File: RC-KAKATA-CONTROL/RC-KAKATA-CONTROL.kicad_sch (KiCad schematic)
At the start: 67 parts, among them J1 Conn_02x20_Socket_DG250T-5.0-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, J10 DB125-2.54-4P-GN, J12 Conn_01x07, J25 Conn_02x20_Socket_DG250T-5.0-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, J6 Raspberry_Pi_2x20_PTH, J8 DB125-2.54-4P-GN, U3 STM32H743IIT6, U8 W25Q128JVSIQTR, X1 SMD3225-4, X2 Q13MC3061000300

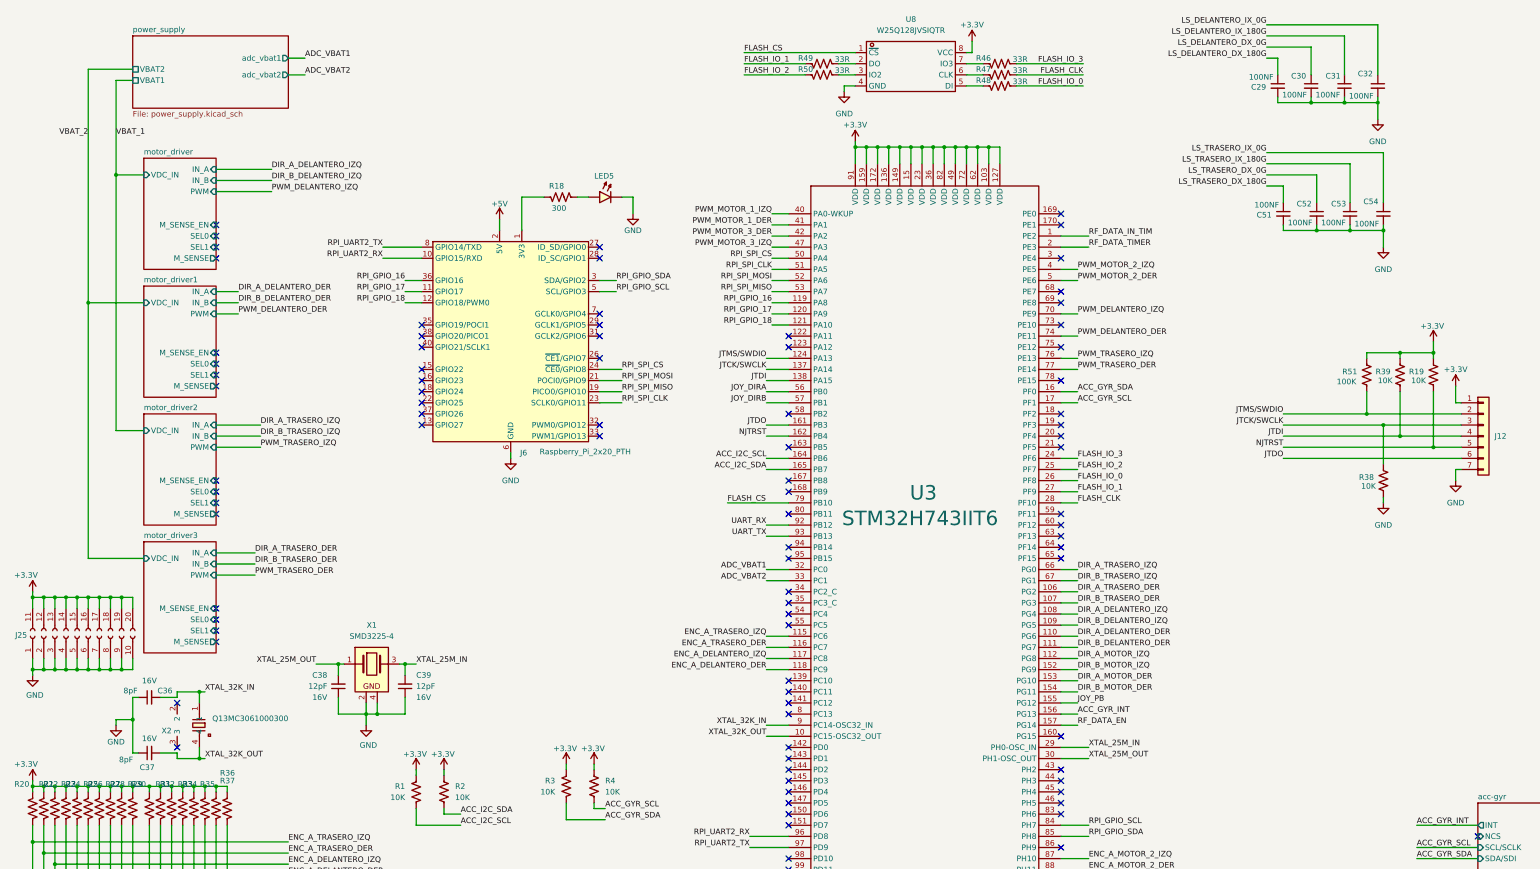
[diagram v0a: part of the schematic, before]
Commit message: Creadas Conexiones de GND y +3.3V Creada Conexion de +5 Creadas las conexiones criticas de Flash - SPI - I2C
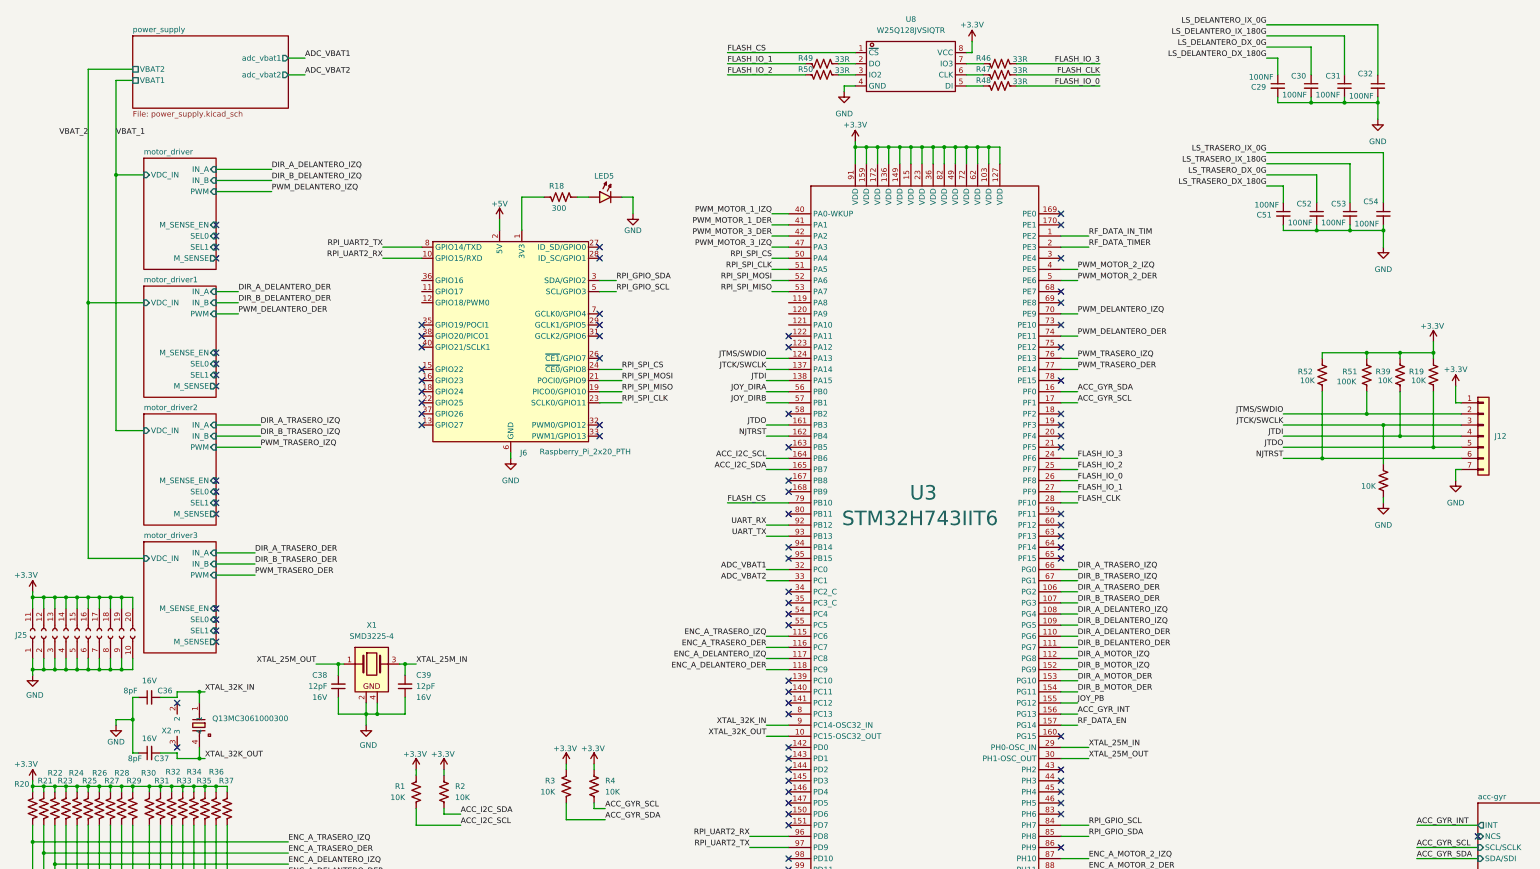
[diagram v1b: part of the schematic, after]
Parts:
- added R52: 10K, 4ms_Resistor:R_0603, symbol MG_RESISTOR:RES-0603-10K-1%
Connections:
- net +3.3V: now also R52.1
- net JTDO: now also J12.5 (Pin_5), R19.2; no longer J12.6 (Pin_6)
- net NJTRST: now also J12.6 (Pin_6), R52.2; no longer J12.5 (Pin_5), R19.2
- net RPI_GPIO_16: no longer names the net of U3.119 (PA8)
- net RPI_GPIO_16: no longer J6.36 (GPIO16)
- net RPI_GPIO_17: no longer names the net of U3.120 (PA9)
- net RPI_GPIO_17: no longer J6.11 (GPIO17)
- net RPI_GPIO_18: no longer names the net of U3.121 (PA10)
- net RPI_GPIO_18: no longer J6.12 (GPIO18/PWM0)

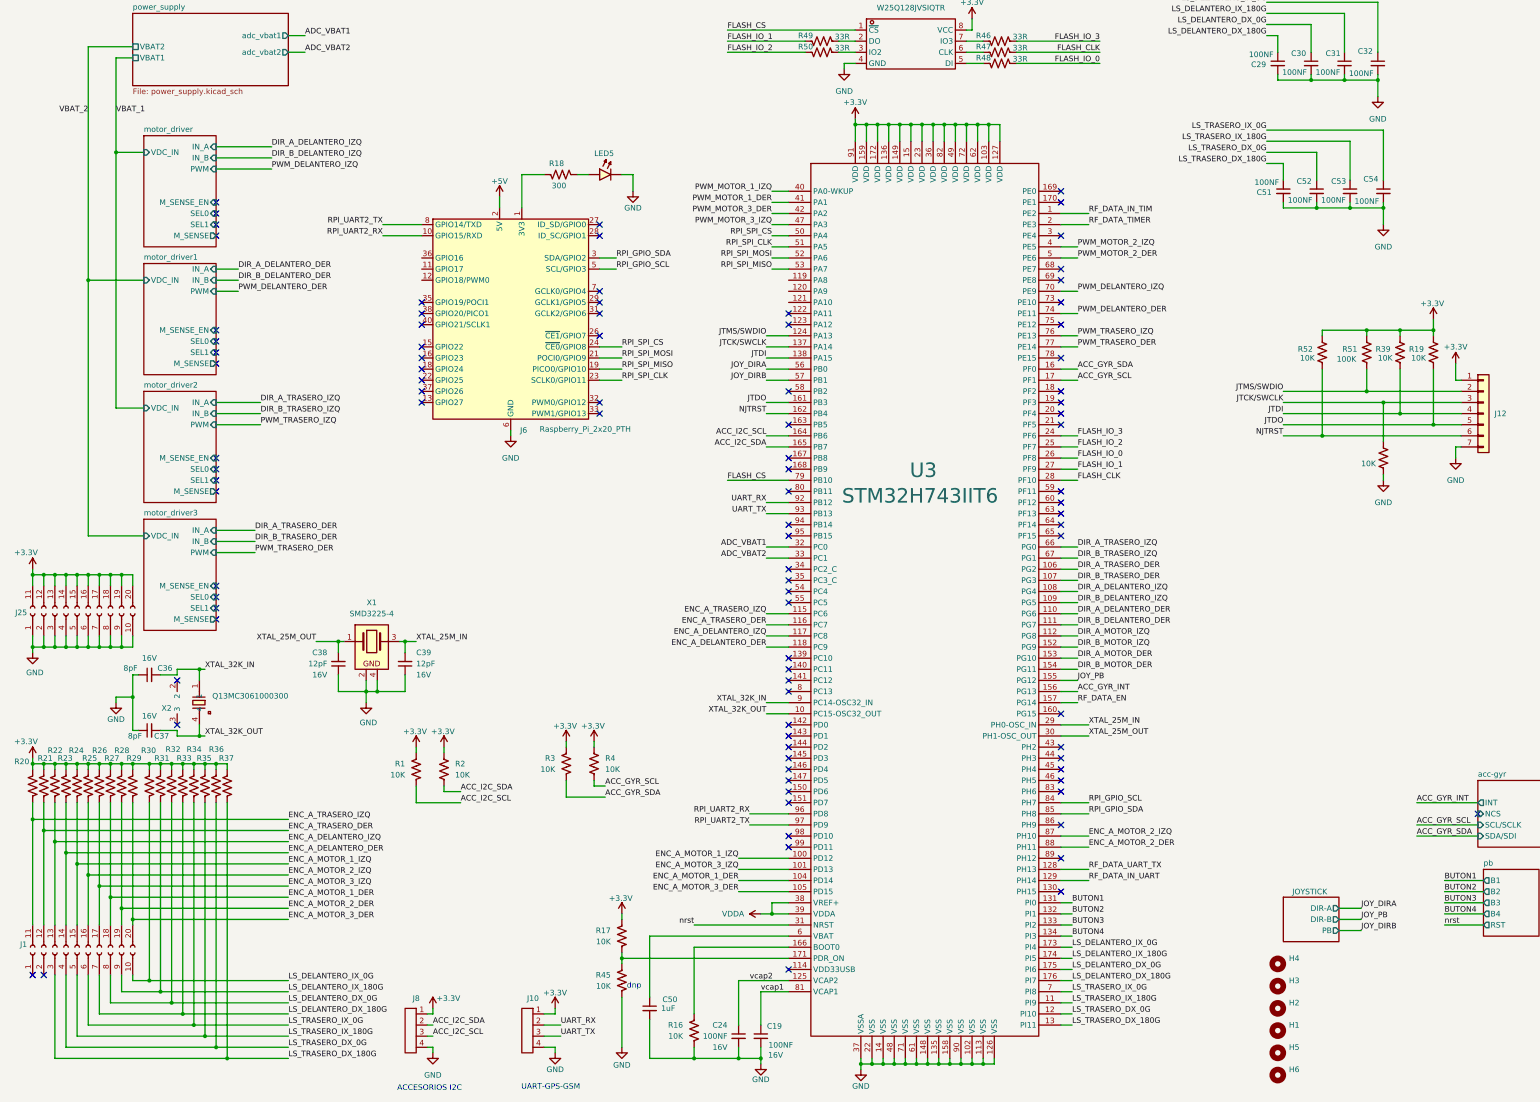
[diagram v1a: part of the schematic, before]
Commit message: Restan 32 pistas por rutear Colocados los Ref de los compoentes
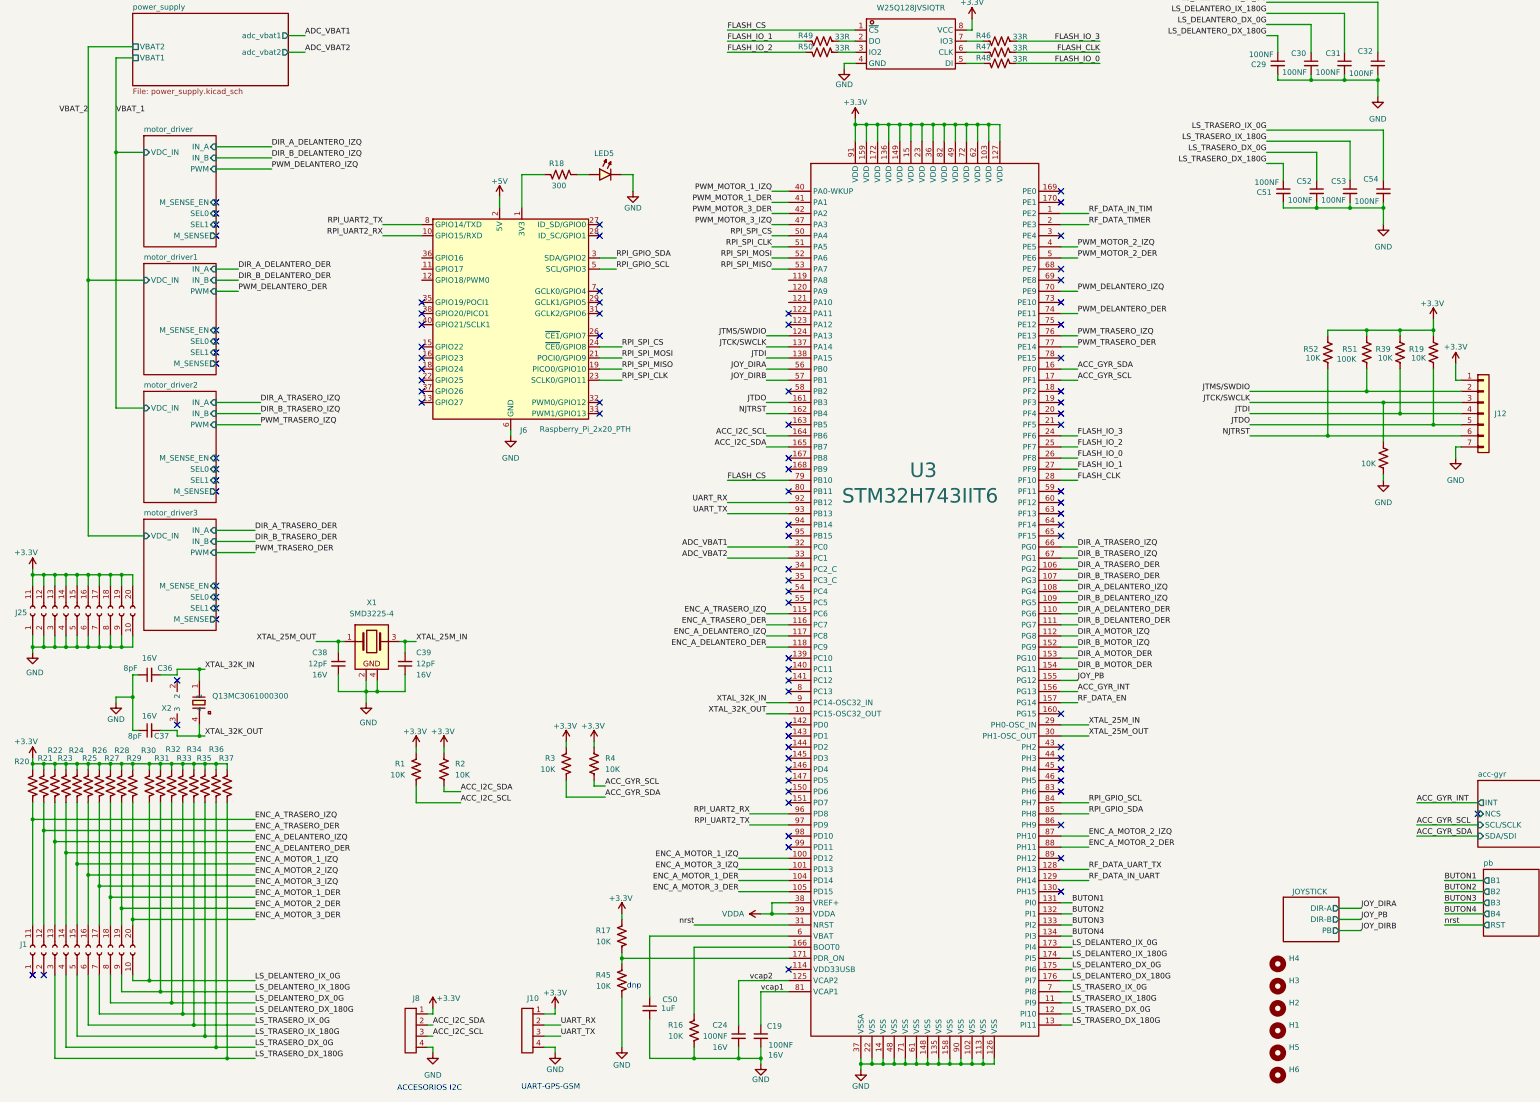
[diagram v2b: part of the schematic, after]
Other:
- moved on the sheet: R52

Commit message: Completado el BOM
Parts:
- added J14: DB125-2.54-4P-GN, EasyEDA:CONN-TH_DB125-2.54-4P-GN, symbol EasyEDA:DB125-2.54-4P-GN
- added R53, R54, R55: 22K, 4ms_Resistor:R_0603, symbol MG_RESISTOR:RES-0603-10K-1%
- added TP1, TP2, TP3, TP4, TP5: TestPoint_Hole1, 4ms_TestPoint:TestPoint_WireHole, symbol MG_ELECTROMECANICAL:TestPoint_Hole1
- C19, C24, C29, C30, C31, C32, C51, C52, C53, C54: LCSC Part (none) -> C14663
- C36: value 8pF -> 16pF; JLCPCB ID C14663 -> (none); LCSC Part (none) -> C327125
- C37: value 8pF -> 16pF; Display 0.1uF -> (none); JLCPCB ID C14663 -> (none); LCSC Part (none) -> C327125
- C38, C39: value 12pF -> 20pF; LCSC Part (none) -> C105621
- C50: LCSC Part (none) -> C559769
- J1, J25: now not fitted; now left out of the parts list
- J6: LCSC Part (none) -> C9138
- LED5: LCSC Part (none) -> C965799
- R1, R2, R3, R4: value 10K -> 4.7K; LCSC Part (none) -> C99782
- R16, R19, R38, R39, R52: LCSC Part (none) -> C98220
- R17: value 10K -> 22K; LCSC Part (none) -> C114065
- R18: LCSC Part (none) -> C114617
- R20, R21, R22, R23, R24, R25, R26, R27, R28, R29, R30, R31, R32, R33, R34, R35, R36, R37: LCSC Part (none) -> C114065
- R45: value 10K -> 22K; LCSC Part (none) -> C114065; now not fitted
- R46, R47, R48: LCSC Part (none) -> C108661
- R49, R50: LCSC Part (none) -> C108661; Part Number RC0603FR-0710KL -> RC0603FR-0733RL
- R51: LCSC Part (none) -> C14675
- U8: value W25Q128JVSIQTR -> W25Q128JVSIQ
- X1: value SMD3225-4 -> 25MHZ; LCSC Part (none) -> C5280577; PART_NUMBER (none) -> XL2EL89CSI-111YLC-25M
- X2: value Q13MC3061000300 -> 32.768kHz; PART_NUMBER (none) -> Q13MC30610003
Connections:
- net +3.3V: now also R53.1, R54.1, R55.1
- net GND: now also J14.4
- net at U3.59 (PF11): now also TP1.1
- net at U3.60 (PF12): now also TP2.1
- net at U3.63 (PF13): now also TP3.1
- net at U3.64 (PF14): now also TP4.1
- net at U3.65 (PF15): now also TP5.1
- net ACC_1: now reaches U3.94 (PB14)
- net ACC_1: now also J14.1, R55.2
- net ACC_2: now reaches U3.98 (PD10)
- net ACC_2: now also J14.2, R54.2
- net ACC_3: now reaches U3.99 (PD11)
- net ACC_3: now also J14.3, R53.2
- no-connect marks 116 -> 108

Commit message: V1.0 Enviada a fabricar
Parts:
- C36: JLCPCB ID (none) -> C14663
- C37: Display (none) -> 0.1uF; JLCPCB ID (none) -> C14663
- J12: LCSC Part (none) -> C6332200
- R49, R50: Part Number RC0603FR-0733RL -> RC0603FR-0710KL
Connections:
- no-connect marks 108 -> 113
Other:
- sheet acc-gyr ports: added SCL, SDA; removed NCS, SCL/SCLK, SDA/SDI
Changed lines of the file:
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@@
 	)
 	(no_connect
+		(at 107.95 81.28)
+	)
+	(no_connect
 		(at 52.07 172.72)
 	)
@@
 	)
 	(no_connect
+		(at 191.77 81.28)
+	)
+	(no_connect
 		(at 191.77 106.68)
 	)
@@
 	)
 	(no_connect
+		(at 107.95 78.74)
+	)
+	(no_connect
 		(at 191.77 129.54)
 	)
 	(no_connect
+		(at 191.77 86.36)
+	)
+	(no_connect
+		(at 191.77 83.82)
+	)
+	(no_connect
 		(at 107.95 86.36)
 	)
@@
 	)
 	(no_connect
-		(at 349.25 203.2)
-	)
-	(no_connect
 		(at 254 63.5)
 	)
@@
 	)
 	(no_connect
+		(at 107.95 76.2)
+	)
+	(no_connect
 		(at 254 213.36)
 	)
@@
 					(size 1.27 1.27)
 				)
+				(hide yes)
 			)
 		)
@@
 			)
 		)
+		(property "LCSC Part" "C6332200"
+			(at 350.52 111.76 0)
+			(effects
+				(font
+					(size 1.27 1.27)
+				)
+				(hide yes)
+			)
+		)
 		(pin "1"
 		)
@@
 					(size 1.27 1.27)
 				)
+				(hide yes)
 			)
 		)
@@
 			)
 		)
-		(property "Part Number" "RC0603FR-0733RL"
+		(property "Part Number" "RC0603FR-0710KL"
 			(at 199.39 29.21 0)
 			(effects
@@
 					(size 1.27 1.27)
 				)
+				(hide yes)
 			)
 		)
@@
 			)
 		)
-		(property "JLCPCB ID" ""
+		(property "JLCPCB ID" "C14663"
 			(at 58.42 170.18 0)
 			(effects
@@
 		)
 		(property "LCSC Part" "C965799"
-			(at 149.86 57.15 0)
+			(at 148.336 61.214 0)
 			(effects
 				(font
 					(size 1.27 1.27)
 				)
+				(hide yes)
 			)
 		)
@@
 			)
 		)
-		(property "Part Number" "RC0603FR-0733RL"
+		(property "Part Number" "RC0603FR-0710KL"
 			(at 199.39 26.67 0)
 			(effects
@@
 					(size 1.27 1.27)
 				)
+				(hide yes)
 			)
 		)
@@
 			)
 		)
-		(property "Display" ""
+		(property "Display" "0.1uF"
 			(at 46.99 182.245 0)
 			(effects
@@
 			)
 		)
-		(property "JLCPCB ID" ""
+		(property "JLCPCB ID" "C14663"
 			(at 58.42 182.88 0)
 			(effects
@@
 		)
 		(property "LCSC Part" "C114617"
-			(at 139.7 57.15 90)
+			(at 137.922 61.976 90)
 			(effects
 				(font
 					(size 1.27 1.27)
 				)
+				(hide yes)
 			)
 		)
@@
 					(size 1.27 1.27)
 				)
+				(hide yes)
 			)
 		)
@@
 				)
 				(justify left top)
+				(hide yes)
 			)
 		)
@@
 			)
 		)
-		(pin "NCS" input
-			(at 349.25 203.2 180)
-			(effects
-				(font
-					(size 1.27 1.27)
-				)
-				(justify left)
-			)
-		)
-		(pin "SCL{slash}SCLK" input
+		(pin "SCL" input
 			(at 349.25 205.74 180)
 			(effects
@@
 			)
 		)
-		(pin "SDA{slash}SDI" input
+		(pin "SDA" bidirectional
 			(at 349.25 208.28 180)
 			(effects
